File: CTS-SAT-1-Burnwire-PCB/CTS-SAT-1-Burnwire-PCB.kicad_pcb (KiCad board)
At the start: 2 copper layers, 50.8 x 22.9 mm, 4 parts

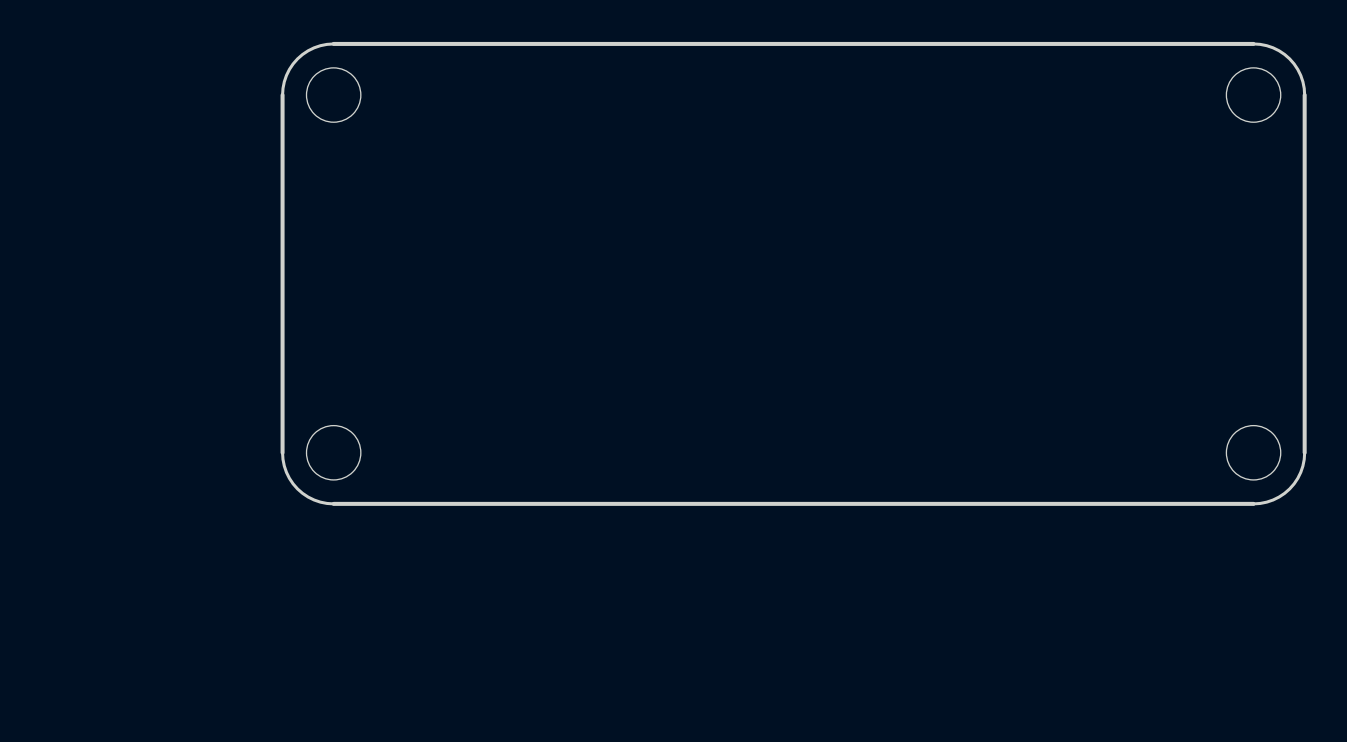
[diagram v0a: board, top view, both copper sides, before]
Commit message: Add board outline, connector locations
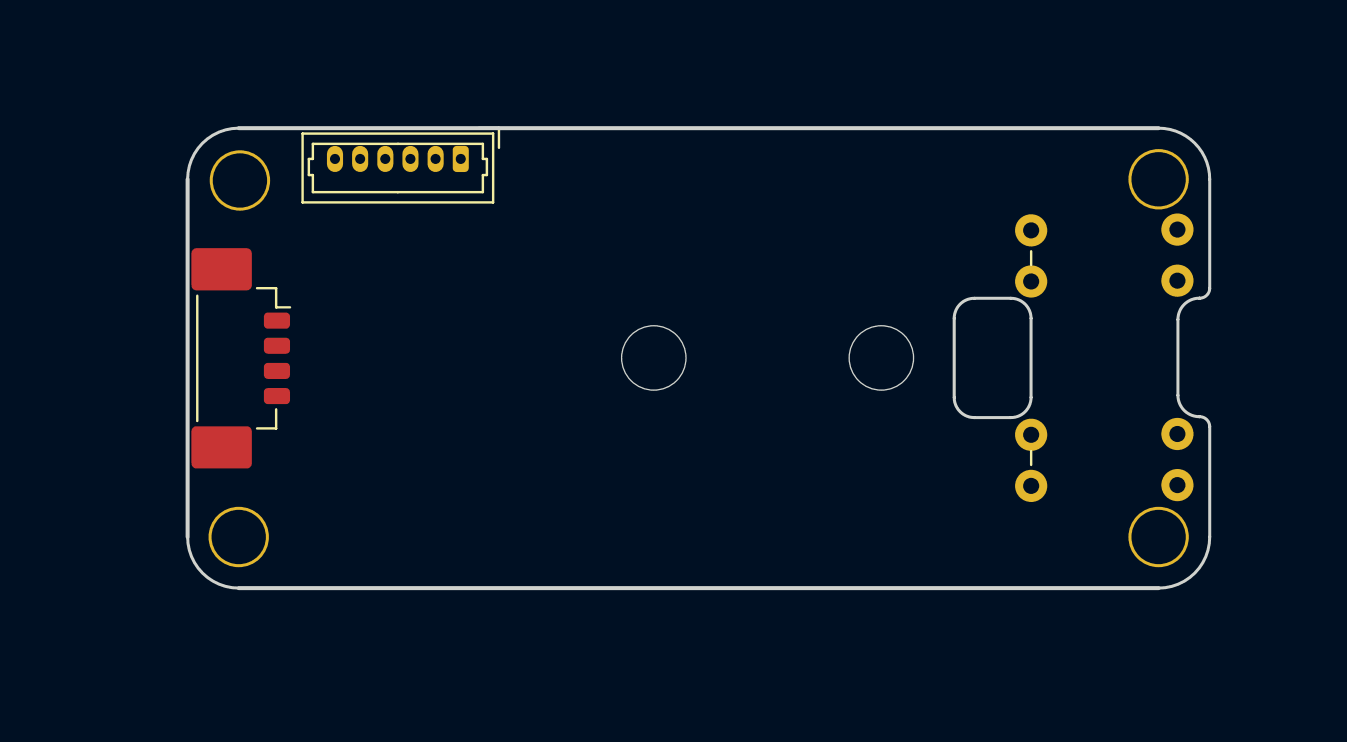
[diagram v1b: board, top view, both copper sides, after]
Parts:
- removed the REF** at (82.9, 52.2)
- removed the REF** at (82.9, 70.0)
- removed the REF** at (128.6, 52.2)
- removed the REF** at (128.6, 70.0)
- added J1: Molex_PicoBlade_53398-0471_1x04-1MP_P1.25mm_Vertical, Connector_Molex:Molex_PicoBlade_53398-0471_1x04-1MP_P1.25mm_Vertical, F.Cu at (78.8, 65.3)
- added J2: Molex_PicoBlade_53047-0610_1x06_P1.25mm_Vertical, Connector_Molex:Molex_PicoBlade_53047-0610_1x06_P1.25mm_Vertical, F.Cu at (89.2, 55.4)
- added R1: 100, Resistor_THT:R_Axial_DIN0207_L6.3mm_D2.5mm_P7.62mm_Horizontal, F.Cu at (117.5, 61.5)
- added R1: 100, Resistor_THT:R_Axial_DIN0309_L9.0mm_D3.2mm_P12.70mm_Horizontal, F.Cu at (117.5, 59.0)
- added R2: 100, Resistor_THT:R_Axial_DIN0207_L6.3mm_D2.5mm_P7.62mm_Horizontal, F.Cu at (124.8, 61.5)
- added REF**: MountingHole_3.2mm_M3, MountingHole:MountingHole_3.2mm_M3, F.Cu at (55.6, 65.3)
- added REF**: MountingHole_2.6mm_M2.5, MountingHole:MountingHole_2.7mm_M2.5, F.Cu at (123.9, 74.2)
- added REF**: MountingHole_2.6mm_M2.5, MountingHole:MountingHole_2.7mm_M2.5, F.Cu at (78.2, 74.2)
- added REF**: MountingHole_2.7mm_M2.5, MountingHole:MountingHole_2.7mm_M2.5, F.Cu at (78.2, 56.5)
- added REF**: MountingHole_3.2mm_M3, MountingHole:MountingHole_3.2mm_M3, F.Cu at (82.8, 65.3)
- added REF**: MountingHole_2.6mm_M2.5, MountingHole:MountingHole_2.7mm_M2.5, F.Cu at (123.9, 56.4)
- added REF**: R_Axial_DIN0309_L9.0mm_D3.2mm_P12.70mm_Horizontal, Resistor_THT:R_Axial_DIN0309_L9.0mm_D3.2mm_P12.70mm_Horizontal, F.Cu at (124.8, 58.9)
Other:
- outline, holes or cut-outs redrawn

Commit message: Layout and routing
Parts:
- removed the R1 at (117.5, 61.5)
- removed the R1 at (117.5, 59.0)
- removed REF** (x2): MountingHole_3.2mm_M3, MountingHole:MountingHole_3.2mm_M3
- removed REF** (x3): MountingHole_2.6mm_M2.5, MountingHole:MountingHole_2.7mm_M2.5
- removed REF**: MountingHole_2.7mm_M2.5, MountingHole:MountingHole_2.7mm_M2.5
- removed REF**: R_Axial_DIN0309_L9.0mm_D3.2mm_P12.70mm_Horizontal, Resistor_THT:R_Axial_DIN0309_L9.0mm_D3.2mm_P12.70mm_Horizontal
- added C1: 10u, Capacitor_SMD:C_1206_3216Metric_Pad1.33x1.80mm_HandSolder, F.Cu at (108.5, 57.5)
- added C2: 100n, Capacitor_SMD:C_1206_3216Metric_Pad1.33x1.80mm_HandSolder, F.Cu at (111.5, 57.5)
- added D1: SMAJ13CA, Diode_SMD:D_SMA, F.Cu at (99.6, 73.4)
- added D2: LED, LED_SMD:LED_0603_1608Metric_Pad1.05x0.95mm_HandSolder, F.Cu at (95.5, 65.1)
- added H1: MountingHole_Pad, MountingHole:MountingHole_2.2mm_M2_Pad, F.Cu at (78.2, 56.5)
- added H2: MountingHole_Pad, MountingHole:MountingHole_2.7mm_M2.5_Pad, F.Cu at (123.9, 56.4)
- added H3: MountingHole_Pad, MountingHole:MountingHole_2.2mm_M2_Pad, F.Cu at (78.2, 74.2)
- added H4: MountingHole_Pad, MountingHole:MountingHole_2.7mm_M2.5_Pad, F.Cu at (123.9, 74.2)
- added Q1: IPD90N04S4L, Package_TO_SOT_SMD:TO-252-3_TabPin2, F.Cu at (102.9, 63.3)
- added R1: R, 00-footprint-lib:AxialBurnResistor, F.Cu at (117.5, 65.3)
- added R3: 100, Resistor_SMD:R_0603_1608Metric_Pad0.98x0.95mm_HandSolder, F.Cu at (89.3, 74.2)
- added R4: 0, Resistor_SMD:R_0603_1608Metric_Pad0.98x0.95mm_HandSolder, F.Cu at (84.7, 62.3)
- added R5: 0, Resistor_SMD:R_0603_1608Metric_Pad0.98x0.95mm_HandSolder, F.Cu at (117.4, 55.1)
- added R6: 0, Resistor_SMD:R_0603_1608Metric_Pad0.98x0.95mm_HandSolder, F.Cu at (83.6, 73.8)
- added R7: 0, Resistor_SMD:R_0603_1608Metric_Pad0.98x0.95mm_HandSolder, F.Cu at (123.2, 69.9)
- added R8: 5k1, Resistor_SMD:R_0603_1608Metric_Pad0.98x0.95mm_HandSolder, F.Cu at (95.6, 69.1)
- added R9: 100k, Resistor_SMD:R_0603_1608Metric_Pad0.98x0.95mm_HandSolder, F.Cu at (84.2, 69.2)
- added S1: Tactile_Button, 00-footprint-lib:SW-SMD_4P-L5.1-W5.1-P3.70-LS6.5-TL-2, F.Cu at (89.9, 66.8)
- J1: value Molex_PicoBlade_53398-0471_1x04-1MP_P1.25mm_Vertical -> Conn_01x04_MountingPin; footprint Connector_Molex:Molex_PicoBlade_53398-0471_1x04-1MP_P1.25mm_Vertical -> Connector_Molex:Molex_PicoBlade_53261-0471_1x04-1MP_P1.25mm_Horizontal
- J2: value Molex_PicoBlade_53047-0610_1x06_P1.25mm_Vertical -> Conn_01x06_MountingPin; footprint Connector_Molex:Molex_PicoBlade_53047-0610_1x06_P1.25mm_Vertical -> Connector_Molex:Molex_PicoBlade_53261-0671_1x06-1MP_P1.25mm_Horizontal
- R2: value 100 -> 5k1; footprint Resistor_THT:R_Axial_DIN0207_L6.3mm_D2.5mm_P7.62mm_Horizontal -> Resistor_SMD:R_0603_1608Metric_Pad0.98x0.95mm_HandSolder
- moved R2 34.0 mm to (93.3, 74.2), turned to 0 degrees
- moved J2 1.97 mm to (90.0, 57.2)
- moved J1 0.09 mm to (78.9, 65.3)
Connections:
- net Vin renamed VDC
- J1 pad 1: IN1 -> GND
- J1 pad 2: IN2 -> GND
- J1 pad 3: EN3V -> BURN_CTRL
- J1 pad 4: EN3V -> Net-(J1-Pin_4)
- J1 pad MP: (no net) -> GND
- R2 pad 2: +5V -> GND
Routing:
- net VDC: track 0.00 -> 40.3 mm
- net Net-(D1-A2): track 0.00 -> 34.2 mm
- net Net-(Q1-D): track 0.00 -> 26.6 mm
- net BURN_CTRL: track 0.00 -> 13.0 mm
- net Net-(H1-Pad1): track 0.00 -> 8.13 mm
- net Net-(H2-Pad1): track 0.00 -> 6.12 mm
- net Net-(H3-Pad1): track 0.00 -> 5.97 mm
- net Net-(H4-Pad1): track 0.00 -> 4.96 mm
- net Net-(D2-K): track 0.00 -> 4.02 mm
- net Net-(J1-Pin_4): track 0.00 -> 3.35 mm
- added copper zone on B.Cu, net GND
- added copper zone on F.Cu, net GND
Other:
- outline, holes or cut-outs redrawn

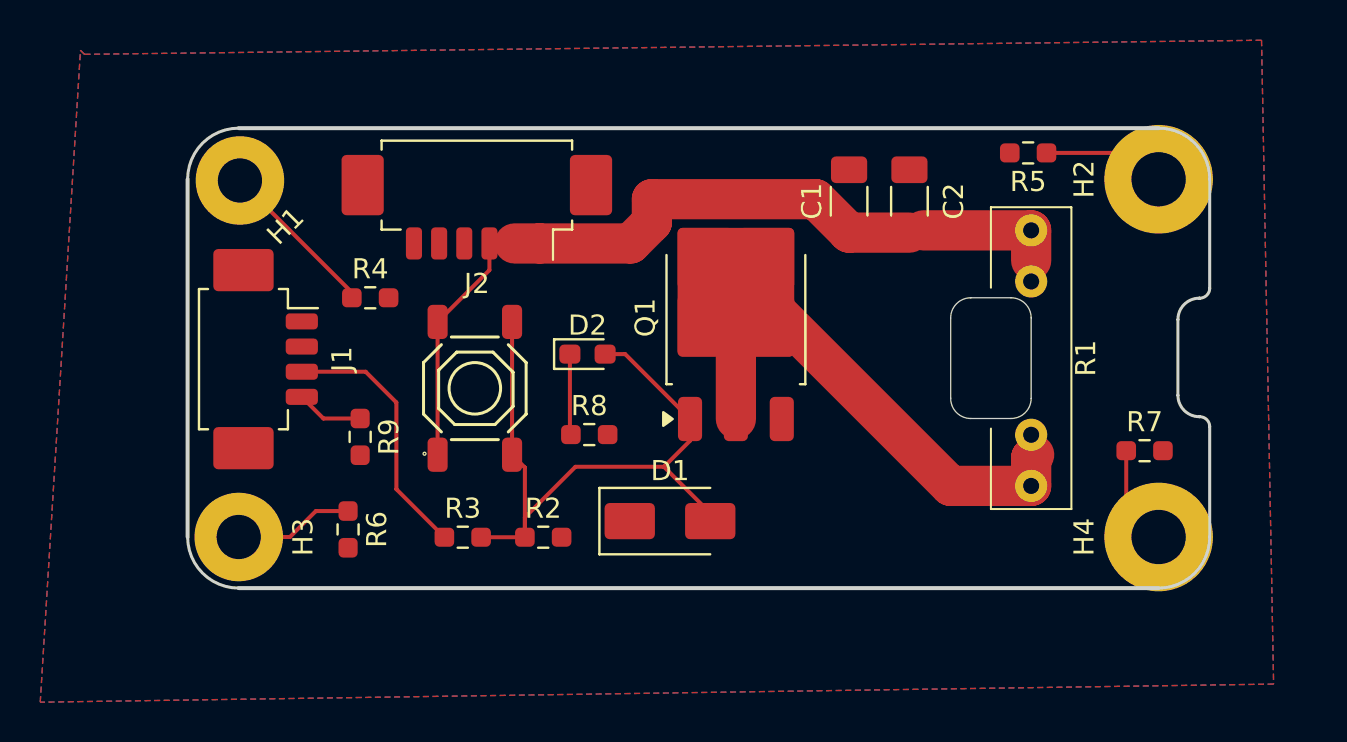
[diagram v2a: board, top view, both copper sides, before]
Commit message: Convert to 2-resistor design
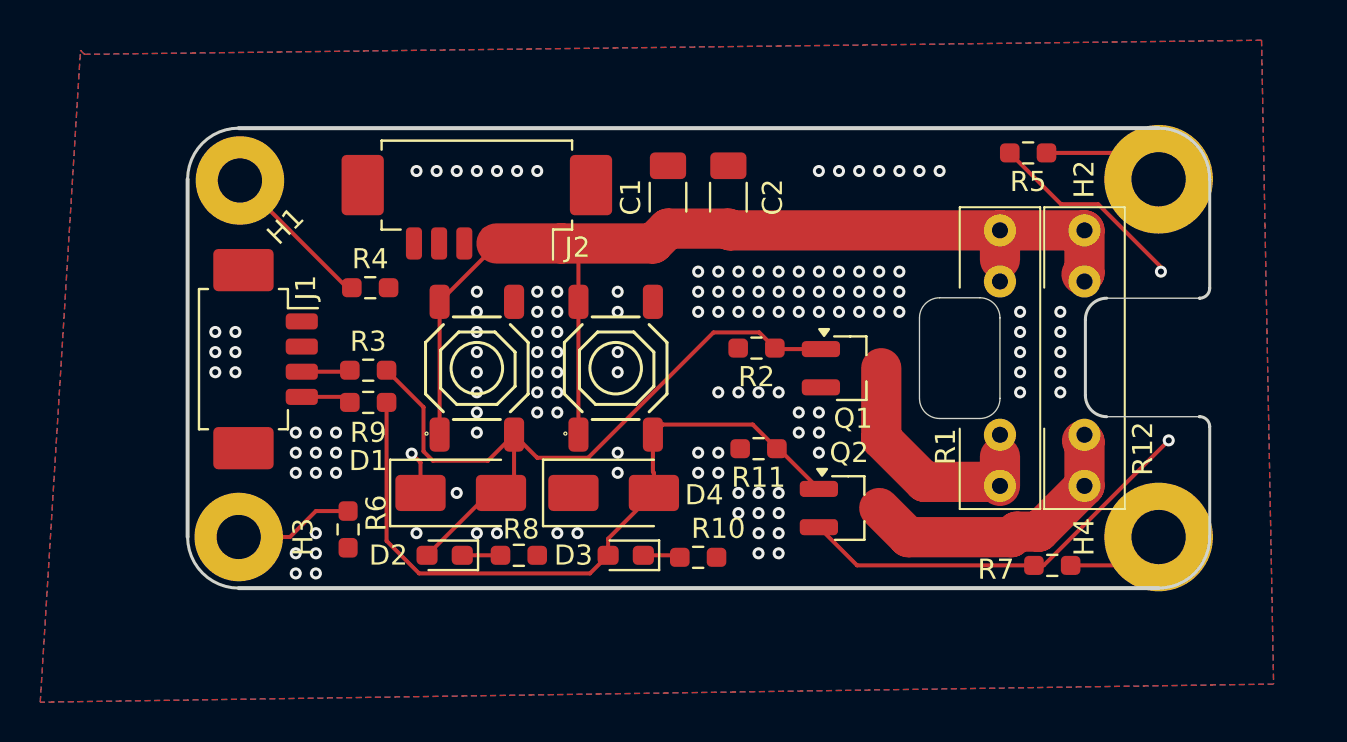
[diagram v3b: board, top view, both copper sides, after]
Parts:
- added D3: LED, LED_SMD:LED_0603_1608Metric_Pad1.05x0.95mm_HandSolder, F.Cu at (97.4, 75.1)
- added D4: SMAJ13CA, Diode_SMD:D_SMA, F.Cu at (96.8, 72.0)
- added Q2: AO3400A, Package_TO_SOT_SMD:SOT-23_Handsoldering, F.Cu at (108.5, 72.8)
- added R10: 5k1, Resistor_SMD:R_0603_1608Metric_Pad0.98x0.95mm_HandSolder, F.Cu at (101.0, 75.2)
- added R11: 5k1, Resistor_SMD:R_0603_1608Metric_Pad0.98x0.95mm_HandSolder, F.Cu at (104.0, 69.8)
- added R12: R, 00-footprint-lib:AxialBurnResistor_No_Cutout, F.Cu at (120.2, 65.3)
- added S2: Tactile_Button, 00-footprint-lib:SW-SMD_4P-L5.1-W5.1-P3.70-LS6.5-TL-2, F.Cu at (96.9, 65.8)
- Q1: value IPD90N04S4L -> AO3400A; footprint Package_TO_SOT_SMD:TO-252-3_TabPin2 -> Package_TO_SOT_SMD:SOT-23_Handsoldering
- R9: value 100k -> 100
- moved R2 14.2 mm to (103.9, 64.8), turned to 180 degrees
- moved D2 12.3 mm to (88.4, 75.1), turned to 180 degrees
- moved D1 10.5 mm to (89.2, 72.0)
- moved R3 9.54 mm to (84.6, 65.9)
- moved C1 9.00 mm to (99.5, 57.3)
- moved C2 9.00 mm to (102.5, 57.3)
- moved R7 7.32 mm to (118.6, 75.6), turned to 180 degrees
- moved R8 6.95 mm to (92.1, 75.1)
- moved Q1 6.25 mm to (108.6, 65.8), turned to 0 degrees
- moved R9 1.76 mm to (84.6, 67.5), turned to 0 degrees
- moved R1 1.55 mm to (116.0, 65.3)
- moved S1 1.00 mm to (90.0, 65.8)
- moved R4 0.50 mm to (84.7, 61.8)
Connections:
- net BURN_CTRL renamed BURN_CTRL_1
- net Net-(J1-Pin_4) renamed BURN_CTRL_2
- Q1 pad 2: Net-(Q1-D) -> GND
- Q1 pad 3: GND -> /Burn_Circuit/BURN_OUT_NEG
- R1 pad 2: Net-(Q1-D) -> /Burn_Circuit/BURN_OUT_NEG
- R9 pad 2: GND -> Net-(D3-A)
- S1 pad 4: Net-(D1-A2) -> unconnected-(S1-D-Pad4)
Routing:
- net Net-(D3-A): track 0.00 -> 35.7 mm
- net GND: track 0.00 -> 33.0 mm, vias 0 -> 137
- net Net-(Q1-D): track 26.6 -> 0.00 mm
- net /Burn_Circuit1/BURN_OUT_NEG: track 0.00 -> 14.2 mm
- net VDC: track 40.3 -> 53.8 mm
- net /Burn_Circuit/BURN_OUT_NEG: track 0.00 -> 11.7 mm
- net BURN_CTRL_1: track 13.0 -> 2.42 mm
- net Net-(D1-A2): track 34.2 -> 36.8 mm
- net Net-(D2-K): track 4.02 -> 1.90 mm
- net Net-(D3-K): track 0.00 -> 1.85 mm
- net Net-(H4-Pad1): track 4.96 -> 6.53 mm
- net BURN_CTRL_2: track 3.35 -> 2.50 mm
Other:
- outline, holes or cut-outs redrawn
- board text added: "CTS-SAT-1 Boom Burn Wire Rev 1 2025-03-18"

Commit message: Remove unnecessary vias
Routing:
- net GND: vias 137 -> 127
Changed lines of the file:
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@@
-	)
-	(via
-		(at 119 64)
-		(size 0.6)
-		(drill 0.3)
-		(layers "F.Cu" "B.Cu")
-		(free yes)
-		(net 1)
-	)
-	(via
-		(at 119 63)
-		(size 0.6)
-		(drill 0.3)
-		(layers "F.Cu" "B.Cu")
-		(free yes)
-		(net 1)
 	)
 	(via
@@
 	)
 	(via
-		(at 117 67)
-		(size 0.6)
-		(drill 0.3)
-		(layers "F.Cu" "B.Cu")
-		(free yes)
-		(net 1)
-	)
-	(via
 		(at 82 76)
 		(size 0.6)
@@
 	)
 	(via
-		(at 119 66)
-		(size 0.6)
-		(drill 0.3)
-		(layers "F.Cu" "B.Cu")
-		(free yes)
-		(net 1)
-	)
-	(via
 		(at 90 62)
 		(size 0.6)
@@
 	)
 	(via
-		(at 119 65)
-		(size 0.6)
-		(drill 0.3)
-		(layers "F.Cu" "B.Cu")
-		(free yes)
-		(net 1)
-	)
-	(via
 		(at 90 65)
 		(size 0.6)
@@
 	)
 	(via
-		(at 119 67)
-		(size 0.6)
-		(drill 0.3)
-		(layers "F.Cu" "B.Cu")
-		(free yes)
-		(net 1)
-	)
-	(via
-		(at 117 66)
-		(size 0.6)
-		(drill 0.3)
-		(layers "F.Cu" "B.Cu")
-		(free yes)
-		(net 1)
-	)
-	(via
 		(at 104 72)
 		(size 0.6)
@@
 	)
 	(via
-		(at 117 63)
-		(size 0.6)
-		(drill 0.3)
-		(layers "F.Cu" "B.Cu")
-		(free yes)
-		(net 1)
-	)
-	(via
 		(at 89 72)
 		(size 0.6)
@@
 	)
 	(via
-		(at 117 64)
-		(size 0.6)
-		(drill 0.3)
-		(layers "F.Cu" "B.Cu")
-		(free yes)
-		(net 1)
-	)
-	(via
 		(at 103 61)
 		(size 0.6)
@@
 		(size 0.6)
 		(drill 0.3)
-		(layers "F.Cu" "B.Cu")
-		(free yes)
-		(net 1)
-	)
-	(via
-		(at 117 65)
-		(size 0.6)
-		(drill 0.3)

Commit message: Add logo, prep release
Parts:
- added REF**: CalgaryToSpace_Logo_20x10mm, 00-footprint-lib:CalgaryToSpace_Logo_20x10mm, B.Cu at (99.0, 65.0)

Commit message: Replace TVS diodes with SMAJ6.5CA
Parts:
- removed REF**: CalgaryToSpace_Logo_20x10mm, 00-footprint-lib:CalgaryToSpace_Logo_20x10mm
- D1, D4: value SMAJ13CA -> SMAJ6.5CA

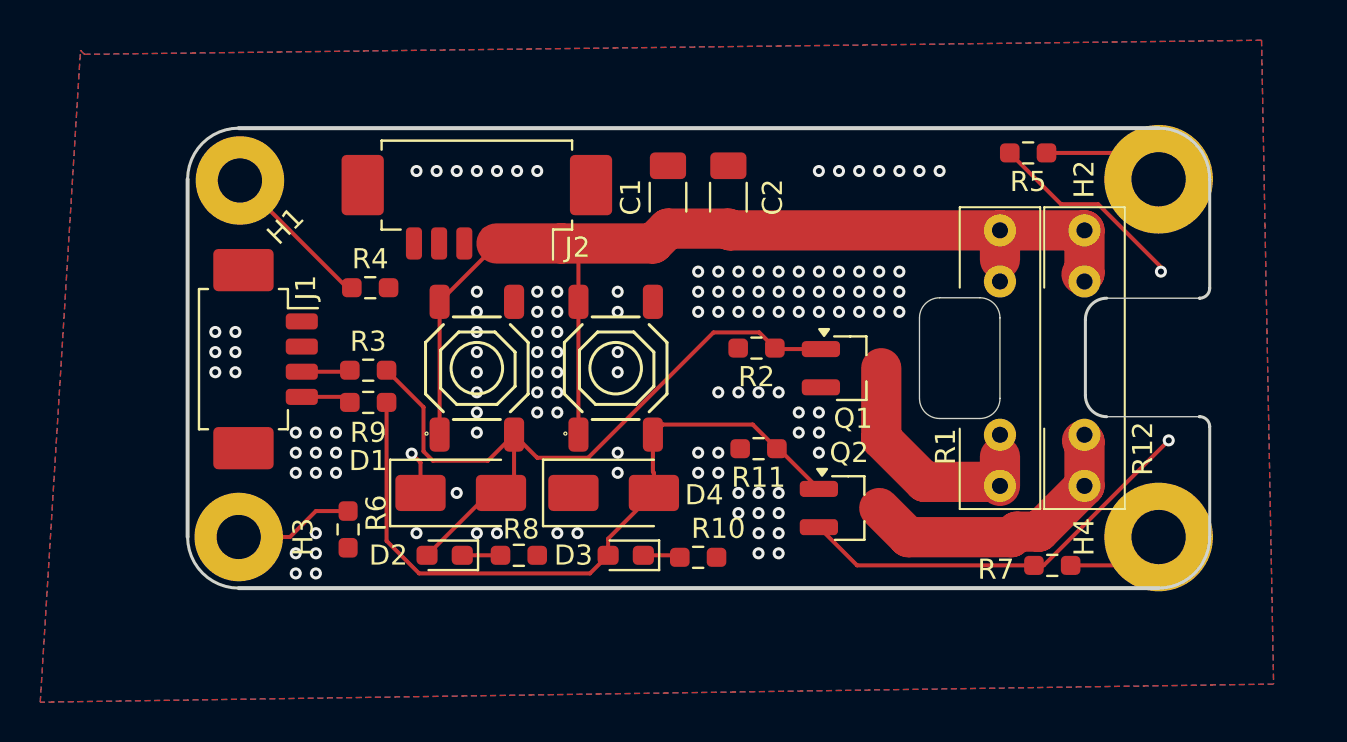
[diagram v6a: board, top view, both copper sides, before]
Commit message: Update mounting hole diameters
M2 by the resistors and M2.5 by the connectors
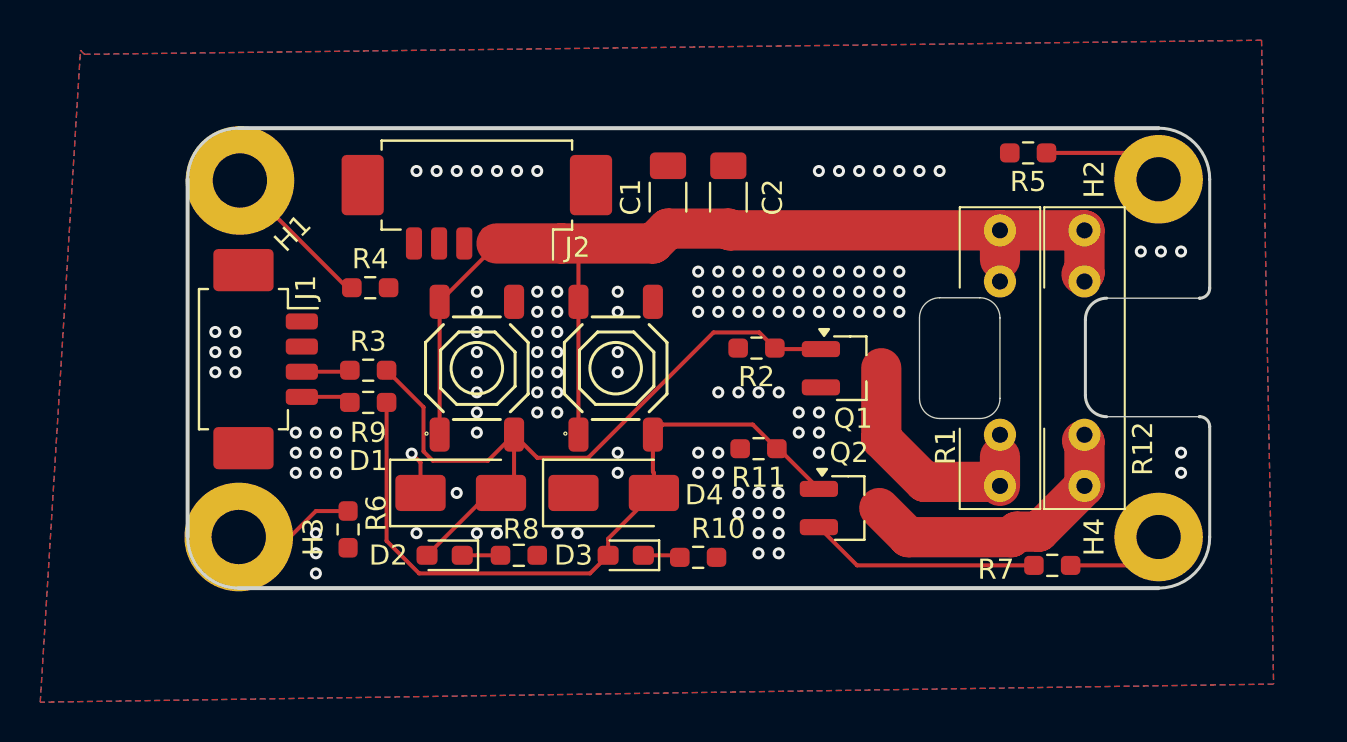
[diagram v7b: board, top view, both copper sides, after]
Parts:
- H1, H3: footprint MountingHole:MountingHole_2.2mm_M2_Pad -> MountingHole:MountingHole_2.7mm_M2.5_Pad
- H2, H4: footprint MountingHole:MountingHole_2.7mm_M2.5_Pad -> MountingHole:MountingHole_2.2mm_M2_Pad
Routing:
- net GND: track 33.0 -> 13.6 mm, vias 127 -> 128
